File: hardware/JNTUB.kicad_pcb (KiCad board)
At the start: 2 copper layers, 70.6 x 128.5 mm, 82 parts, among them J1 PARAM1_CV, J10 B2_HDR_LEFT, J11 B2_HDR_RIGHT, J2 PARAM2_CV, J3 CLK/TRG, J4 DITTO, J5 OUT1, J6 OUT2, J7 B1_HDR_LEFT, J8 B1_HDR_RIGHT, J9 POWER, Q1 2N3904, Q2 2N3904, Q3 2N3904, U1 ATtiny85, U2 TL074, U3 78L05, U4 79L05

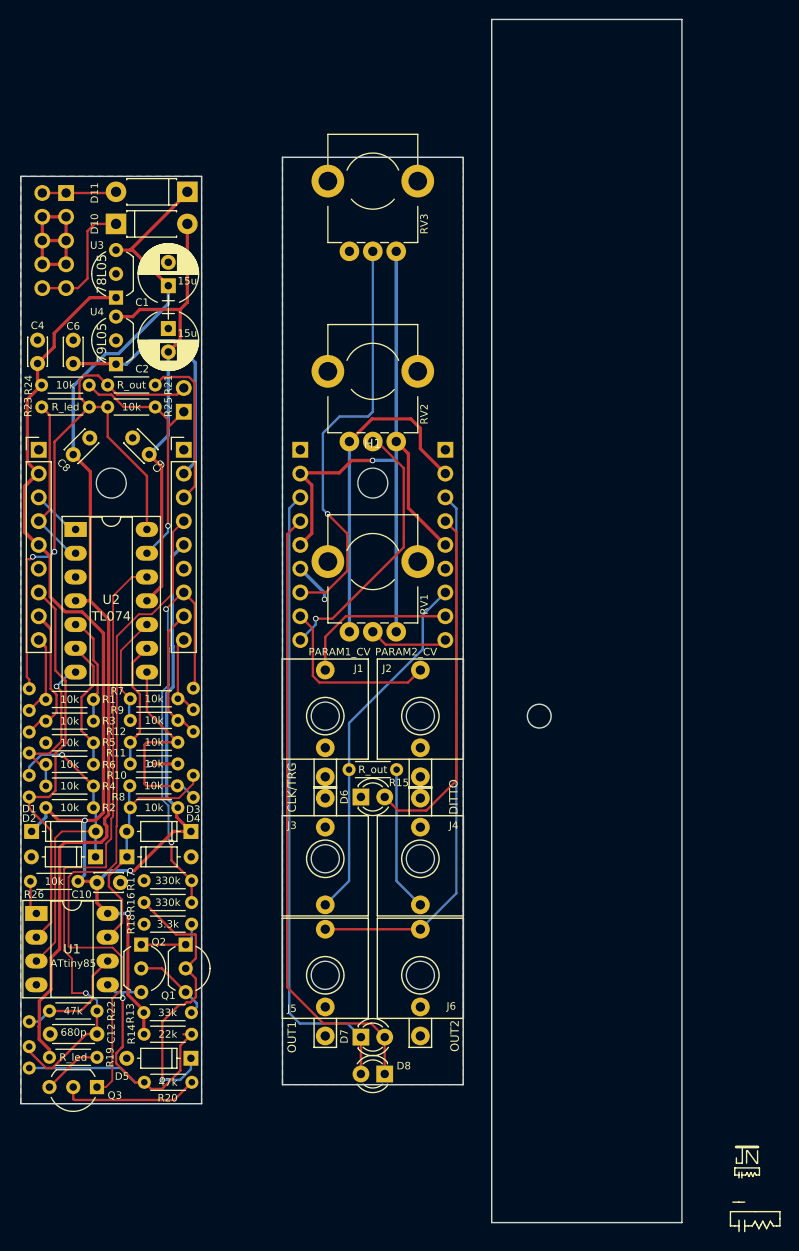
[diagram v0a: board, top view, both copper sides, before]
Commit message: [JNTUB-HW] Overhaul PCB layout
- Make traces and clearances much bigger than first attempt
- Remove test points and resistor leading to MCU RESET
- Move some resistors to peripheral board
- Space out remaining components on main board
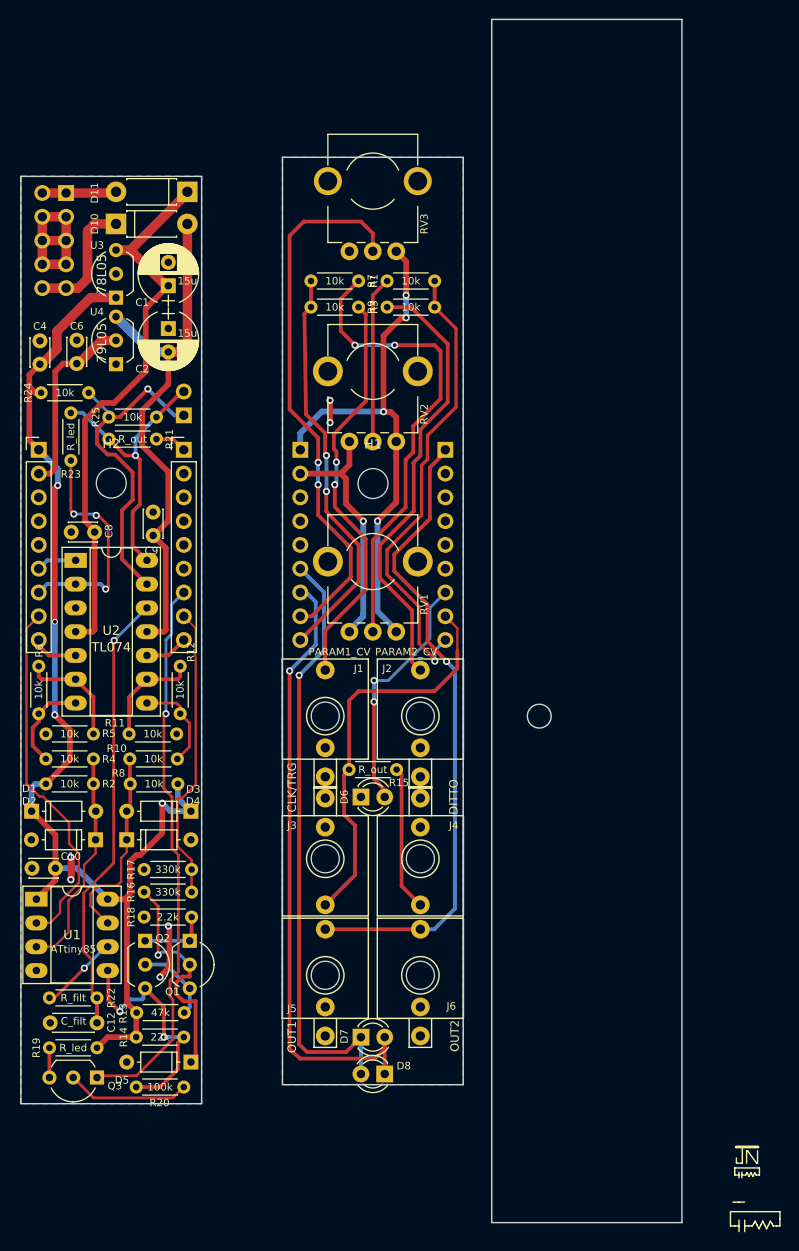
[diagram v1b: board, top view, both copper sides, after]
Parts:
- removed R26: 10k, SDIY:R_Axial_DIN0204_L3.6mm_D1.6mm_P5.08mm_Horizontal
- removed TP1: P3_FIN, SDIY:Test_Point
- removed TP10: TRG_FIN, SDIY:Test_Point
- removed TP11: CLK/TRG, SDIY:Test_Point
- removed TP12: OUT, SDIY:Test_Point
- removed TP13: PWM_RAW, SDIY:Test_Point
- removed TP14: PWM_FILT, SDIY:Test_Point
- removed TP2: P2_POT, SDIY:Test_Point
- removed TP3: P2_CV, SDIY:Test_Point
- removed TP4: P2_FIN, SDIY:Test_Point
- removed TP5: P2_SUM, SDIY:Test_Point
- removed TP6: P1_POT, SDIY:Test_Point
- removed TP7: P1_CV, SDIY:Test_Point
- removed TP8: P1_FIN, SDIY:Test_Point
- removed TP9: P1_SUM, SDIY:Test_Point
- C12: value 680p -> C_filt
- H1, H2: value MountingHole_3.2mm_M3 -> MountingHole
- R13: value 33k -> 47k
- R18: value 3.3k -> 2.2k
- R20: value 47k -> 100k
- R22: value 47k -> R_filt
- moved R1 57.7 mm to (235.2, 69.1)
- moved R3 57.3 mm to (235.2, 71.9)
- moved R7 48.6 mm to (232.2, 69.1)
- moved R9 48.2 mm to (232.2, 71.9)
- moved C8 8.59 mm to (204.0, 95.9), turned to 180 degrees
- moved C9 8.22 mm to (210.2, 93.8), turned to 270 degrees
- moved R21 5.78 mm to (210.6, 86.0)
- moved R6 5.46 mm to (198.0, 115.3), turned to 90 degrees
- moved R19 5.18 mm to (199.1, 151.0), turned to 0 degrees
- moved R25 5.07 mm to (205.5, 83.6), turned to 0 degrees
- moved C10 4.70 mm to (199.8, 131.8), turned to 180 degrees
- moved U2 3.30 mm to (201.9, 98.9)
- moved R11 3.20 mm to (207.6, 117.5)
- moved R12 3.06 mm to (213.1, 115.3), turned to 90 degrees
- moved R4 2.90 mm to (198.8, 120.1)
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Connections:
- J10 pad 1: GNDREF -> +5V
- J10 pad 2: +5V -> -5V
- J10 pad 3: /MainBoard/OUT_LED- -> GNDREF
- J10 pad 4: /MainBoard/OUT_LED+ -> GNDREF
- J10 pad 5: +5V -> GNDREF
- J10 pad 6: GNDREF -> /MainBoard/OUT_LED-
- J10 pad 7: /MainBoard/MCU_ADC3 -> /MainBoard/OUT_LED+
- J10 pad 8: /MainBoard/P2_CV -> /MainBoard/MCU_ADC3
- J10 pad 9: /MainBoard/P2_POT -> /MainBoard/P1_AVG
- J11 pad 1: GNDREF -> /MainBoard/OUT
- J11 pad 2: -5V -> GNDREF
- J11 pad 3: /MainBoard/OUT -> GNDREF
- J11 pad 4: /MainBoard/IN_LED+ -> GNDREF
- J11 pad 5: +5V -> GNDREF
- J11 pad 6: Net-(J11-Pad6) -> GNDREF
- J11 pad 7: /MainBoard/CLK_TRG -> /MainBoard/IN_LED+
- J11 pad 8: /MainBoard/P1_CV -> /MainBoard/CLK_TRG
- J11 pad 9: /MainBoard/P1_POT -> /MainBoard/P2_AVG
- J7 pad 1: GNDREF -> +5V
- J7 pad 2: +5V -> -5V
- J7 pad 3: /PeripheralBoard/OUT_LED- -> GNDREF
- J7 pad 4: /PeripheralBoard/OUT_LED+ -> GNDREF
- J7 pad 5: +5V -> GNDREF
- J7 pad 6: GNDREF -> /PeripheralBoard/OUT_LED-
- J7 pad 7: /PeripheralBoard/P3_POT -> /PeripheralBoard/OUT_LED+
- J7 pad 8: /PeripheralBoard/P2_CV -> /PeripheralBoard/P3_POT
- J7 pad 9: /PeripheralBoard/P2_POT -> /PeripheralBoard/P1_AVG
- J8 pad 1: GNDREF -> /PeripheralBoard/OUT
- J8 pad 2: -5V -> GNDREF
- J8 pad 3: /PeripheralBoard/OUT -> GNDREF
- J8 pad 4: /PeripheralBoard/IN_LED+ -> GNDREF
- J8 pad 5: +5V -> GNDREF
- J8 pad 6: Net-(J8-Pad6) -> GNDREF
- J8 pad 7: /PeripheralBoard/CLK_TRG -> /PeripheralBoard/IN_LED+
- J8 pad 8: /PeripheralBoard/P1_CV -> /PeripheralBoard/CLK_TRG
- J8 pad 9: /PeripheralBoard/P1_POT -> /PeripheralBoard/P2_AVG
- R1 pad 1: /MainBoard/P2_POT -> /PeripheralBoard/P2_POT
- R1 pad 2: Net-(R1-Pad2) -> /PeripheralBoard/P2_AVG
- R19 pad 2: +12V -> +5V
- R3 pad 1: /MainBoard/P2_CV -> /PeripheralBoard/P2_CV
- R3 pad 2: Net-(R1-Pad2) -> /PeripheralBoard/P2_AVG
- R7 pad 1: /MainBoard/P1_POT -> /PeripheralBoard/P1_POT
- R7 pad 2: Net-(R7-Pad2) -> /PeripheralBoard/P1_AVG
- R9 pad 1: /MainBoard/P1_CV -> /PeripheralBoard/P1_CV
- R9 pad 2: Net-(R7-Pad2) -> /PeripheralBoard/P1_AVG
- RV1 pad 4: (no net) -> GNDREF
- RV2 pad 4: (no net) -> GNDREF
- RV3 pad 4: (no net) -> GNDREF
- U1 pad 1: Net-(R26-Pad2) -> +5V
- U2 pad 10: Net-(R7-Pad2) -> /MainBoard/P2_AVG
- U2 pad 5: Net-(R1-Pad2) -> /MainBoard/P1_AVG
- U4 pad 1: -5V -> GNDREF
- U4 pad 2: GNDREF -> -5V
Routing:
- net +12V: track 112.5 -> 59.6 mm
- net /PeripheralBoard/P2_AVG: track 0.00 -> 49.4 mm, vias 0 -> 1
- net /PeripheralBoard/P1_AVG: track 0.00 -> 43.5 mm, vias 0 -> 2
- net /PeripheralBoard/P1_POT: track 9.15 -> 50.7 mm, vias 0 -> 2
- net +5V: track 223.7 -> 182.5 mm, vias 4 -> 8
- net Net-(JP1-Pad2): track 66.8 -> 30.2 mm, vias 2 -> 1
- net /PeripheralBoard/P2_CV: track 19.3 -> 48.8 mm
- net /PeripheralBoard/P1_CV: track 17.3 -> 43.8 mm, vias 0 -> 2
- net Net-(C12-Pad1): track 68.4 -> 48.7 mm
- net /MainBoard/P2_CV: track 16.9 -> 0.00 mm
- net /MainBoard/IN_LED+: track 75.1 -> 59.5 mm, vias 0 -> 1
- net -5V: track 62.7 -> 47.7 mm, vias 0 -> 1
- net /MainBoard/CLK_TRG: track 46.5 -> 31.7 mm, vias 2 -> 0
- net /MainBoard/P1_CV: track 14.4 -> 0.00 mm
- net /MainBoard/OUT: track 17.6 -> 3.39 mm
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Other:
- net class Default: clearance 0.2 -> 0.3048; trace_width 0.25 -> 0.4064; via_dia 0.6 -> 0.762; via_drill 0.4 -> 0.4064
- net class Medium added: clearance 0.3048, trace_width 0.3048, via_dia 0.762, via_drill 0.4064
- net class Power: clearance 0.2 -> 0.508; trace_width 0.35 -> 0.6096; via_dia 0.6 -> 0.762; via_drill 0.4 -> 0.4064
- net class Small added: clearance 0.3048, trace_width 0.254, via_dia 0.762, via_drill 0.4064
- net class Small and Close added: clearance 0.254, trace_width 0.254, via_dia 0.762, via_drill 0.4064
- rule pad_to_mask_clearance: 0.2 -> 0.2032
- rule trace_clearance: 0.2 -> 0.3048
- rule trace_min: 0.2 -> 0.2032

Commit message: [JNTUB-HW] Clean up PCB v0.1 for fabrication
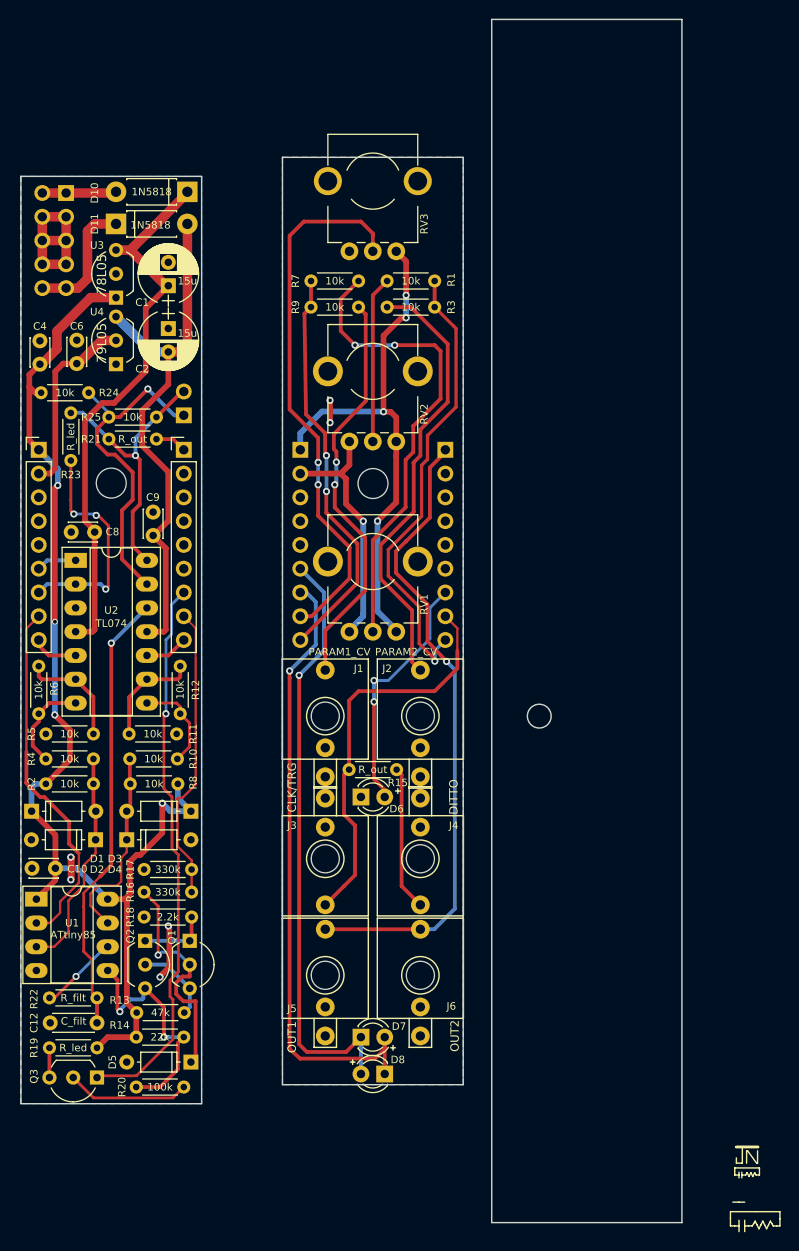
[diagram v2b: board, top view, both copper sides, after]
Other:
- board text added: "Board 1 of 2"
- board text added: "Board 2 of 2"
- board text added: "Dec. 2020"
- board text added: "JoyfulNoise Tiny Utility Board"
- board text added: "Rev 0.1"
- board text added: "Set for 0-5V OUT"
- board text removed: "JoyfulNoise Tiny Utility Board Rev 0.1 — Dec. 2020 Board 1 of 2"

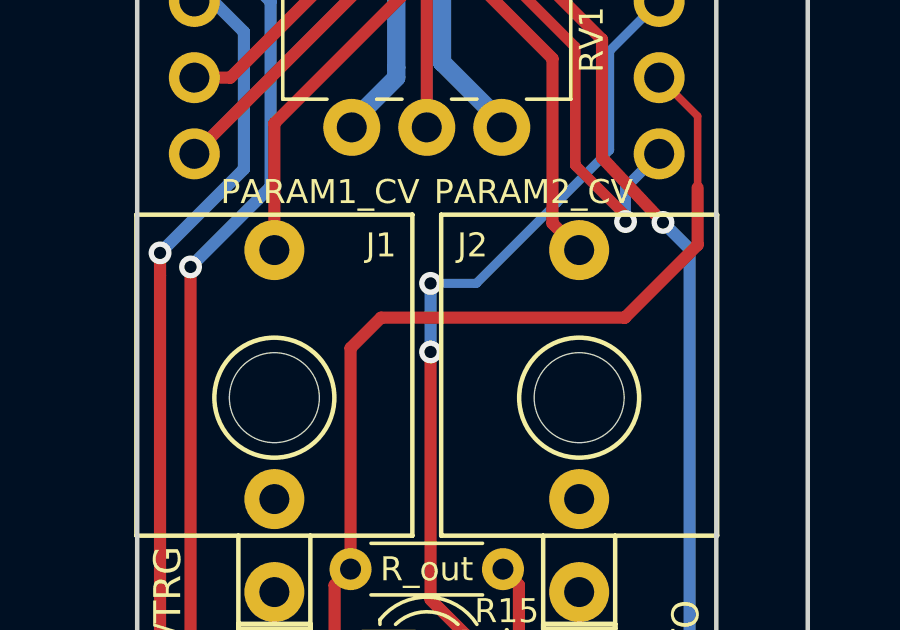
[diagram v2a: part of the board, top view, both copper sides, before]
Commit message: [JNTUB-HW] Write script to copy PCB for splitting
Need to have separate Gerber files for each board.
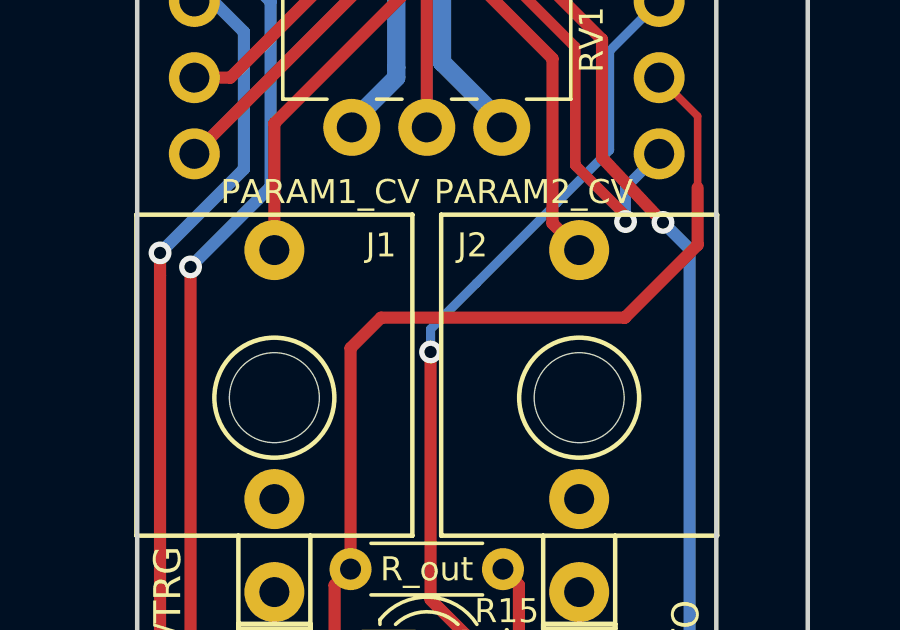
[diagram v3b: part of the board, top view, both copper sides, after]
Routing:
- net /PeripheralBoard/IN_LED+: track 26.9 -> 26.0 mm, vias 2 -> 1
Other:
- rule pad_to_mask_clearance: 0.2032 -> 0
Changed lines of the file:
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@@
     (thickness 1.6)
     (drawings 161)
-    (tracks 550)
+    (tracks 549)
     (zones 0)
     (modules 67)
@@
     (pad_size 2.999999 2.999999)
     (pad_drill 2)
-    (pad_to_mask_clearance 0.2032)
+    (pad_to_mask_clearance 0)
     (aux_axis_origin 0 0)
     (visible_elements FFFFFF7F)
@@
   (segment (start 233.807 114.046) (end 233.807 122.301) (width 0.4064) (layer F.Cu) (net 30))
   (via (at 233.807 114.046) (size 0.762) (drill 0.4064) (layers F.Cu B.Cu) (net 30))
-  (segment (start 233.807 114.046) (end 233.807 111.76) (width 0.4064) (layer B.Cu) (net 30))
-  (via (at 233.807 111.76) (size 0.762) (drill 0.4064) (layers F.Cu B.Cu) (net 30))
   (segment (start 241.427 102.362) (end 241.427 102.892158) (width 0.4064) (layer B.Cu) (net 30))
-  (segment (start 235.331 111.76) (end 233.807 111.76) (width 0.3048) (layer B.Cu) (net 30))
   (segment (start 237.998 109.093) (end 235.331 111.76) (width 0.3048) (layer B.Cu) (net 30))
   (segment (start 241.427 102.362) (end 239.776 104.013) (width 0.3048) (layer B.Cu) (net 30))
   (segment (start 237.998 109.093) (end 239.776 107.315) (width 0.3048) (layer B.Cu) (net 30))
   (segment (start 239.776 104.013) (end 239.776 107.315) (width 0.3048) (layer B.Cu) (net 30))
+  (segment (start 233.807 113.284) (end 233.807 114.046) (width 0.3048) (layer B.Cu) (net 30))
+  (segment (start 235.331 111.76) (end 233.807 113.284) (width 0.3048) (layer B.Cu) (net 30))
   (segment (start 232.41 149.86) (end 232.41 153.797) (width 0.4064) (layer B.Cu) (net 31))
   (segment (start 226.631201 151.447201) (end 230.822799 151.447201) (width 0.4064) (layer F.Cu) (net 31))

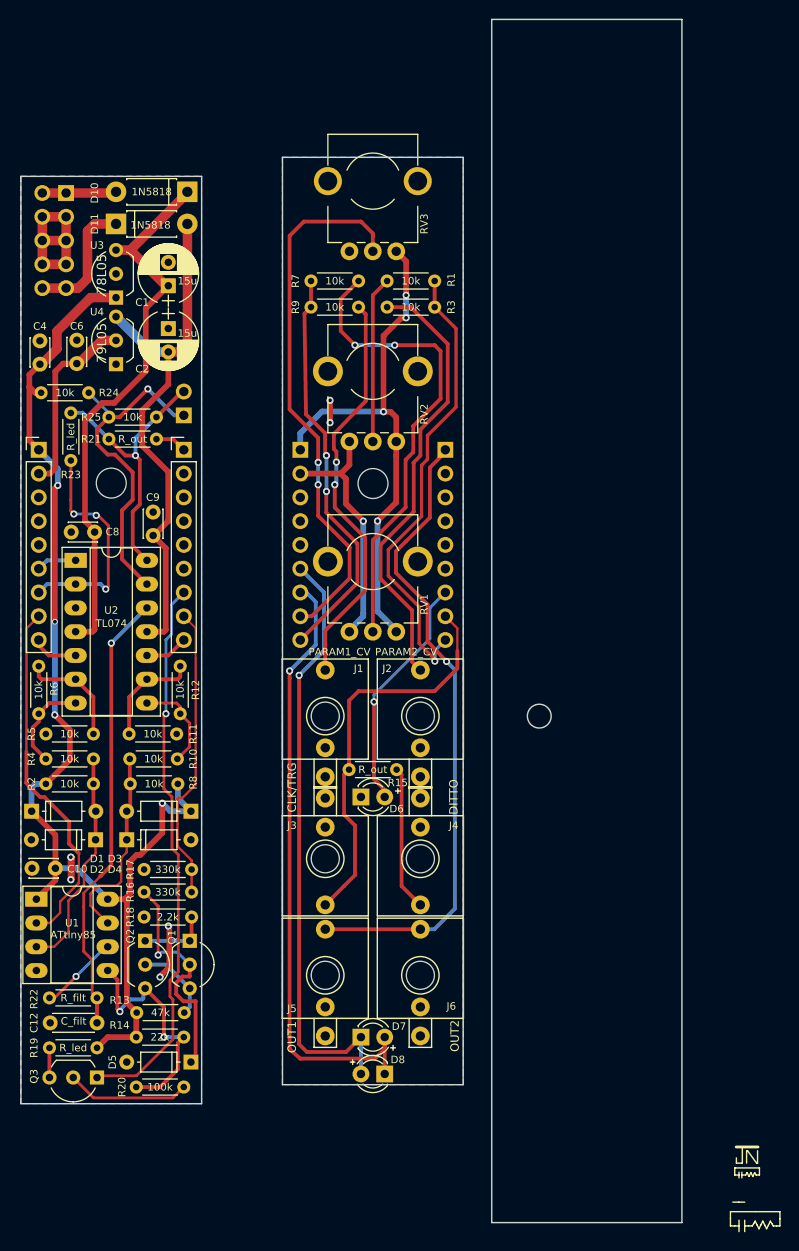
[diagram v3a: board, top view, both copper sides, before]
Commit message: [JNTUB-HW] Swap front and back copper layers
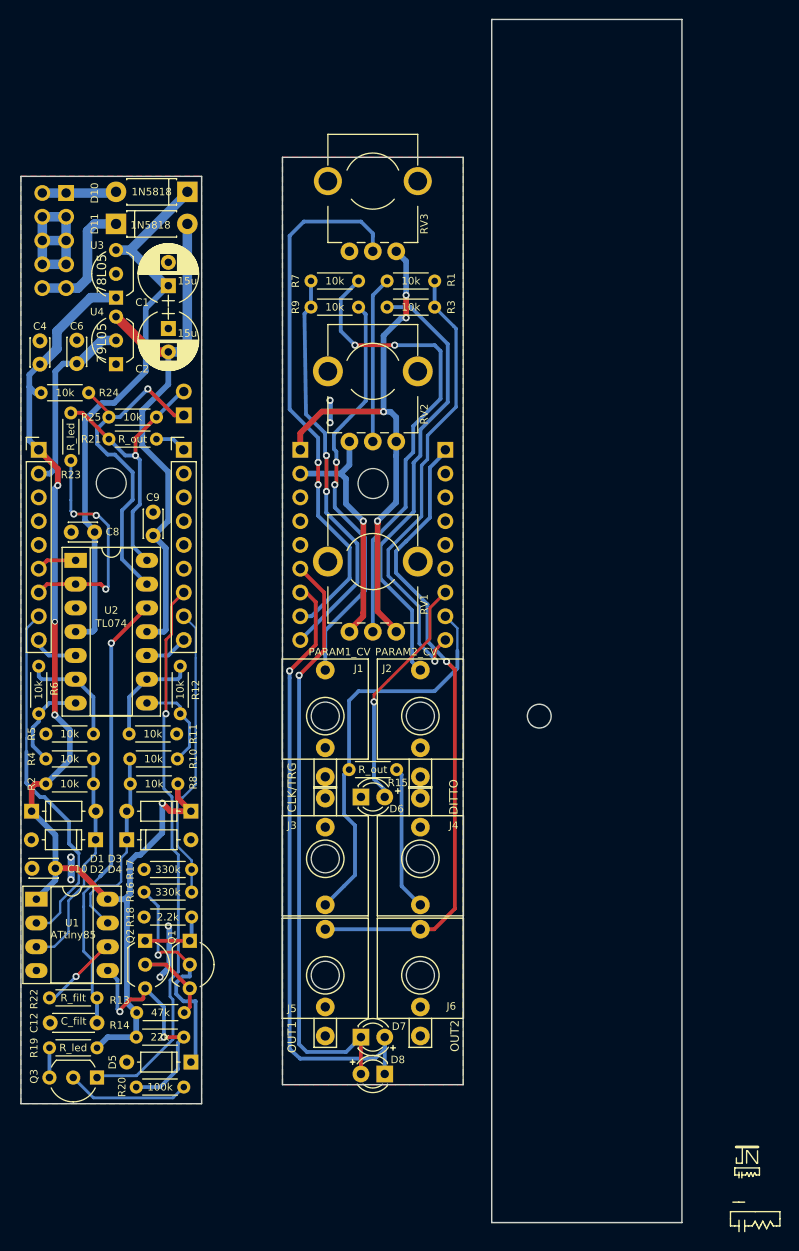
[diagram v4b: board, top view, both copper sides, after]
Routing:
- added copper zone on F.Cu, net GNDREF
- removed copper zone on B.Cu, net GNDREF
